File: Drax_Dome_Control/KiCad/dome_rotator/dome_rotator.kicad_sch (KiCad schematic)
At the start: 22 parts, among them J1 Screw_Terminal_01x16, J2 Conn_01x16_Female, Q1 2N2222, SW1 SW_Reed, U1 SFH617A-1, U2 SFH617A-1

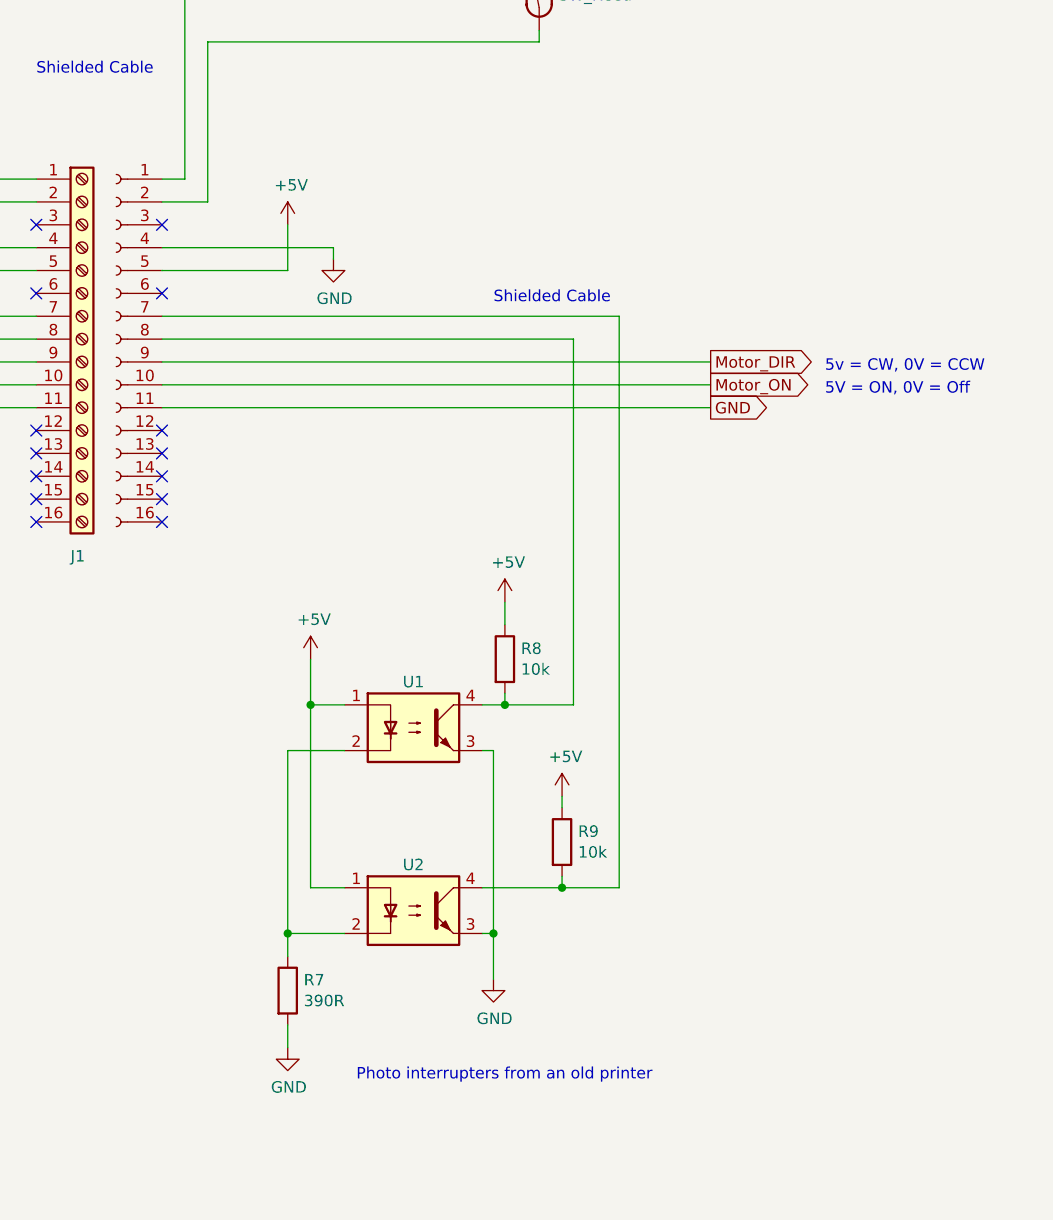
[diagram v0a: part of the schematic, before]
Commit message: Drax_Dome_Control: added debug and started testing
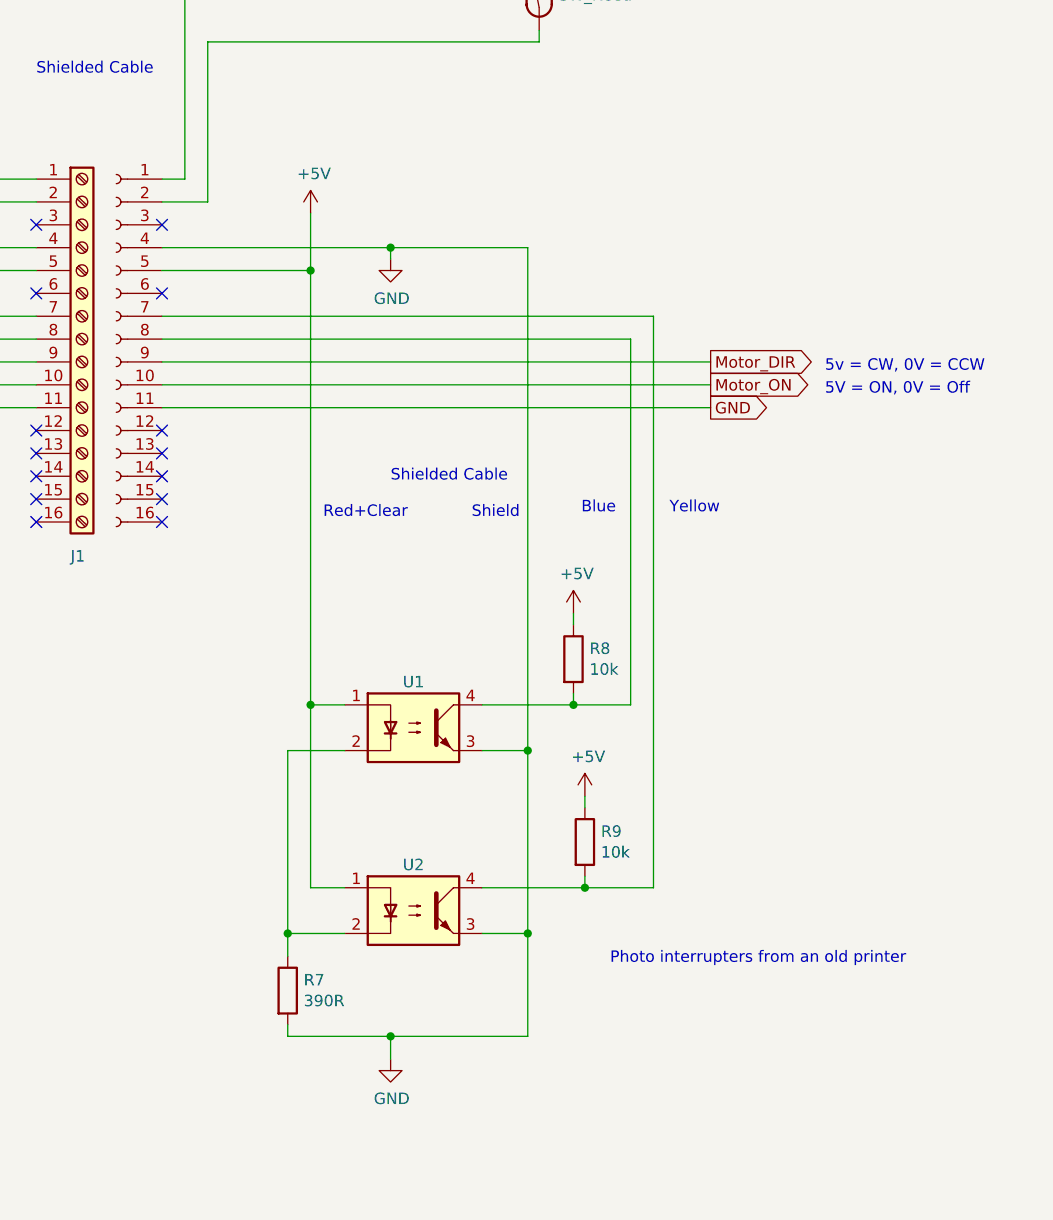
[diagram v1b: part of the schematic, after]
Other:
- note added: "Blue"
- note added: "Red+Clear"
- note added: "Shield"
- note added: "Yellow"
- moved on the sheet: R8, R9
